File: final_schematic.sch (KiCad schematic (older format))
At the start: 59 parts, among them J1 USB_B_Micro, J2 Conn_Coaxial, J3 Conn_01x04_Male, U1 BQ27441-G1, U2 BQ24075, U3 MTK3339, U4 XC6220B331MR, U5 XC6220B331MR, U6 STM32L476VGTx, U7 RFM95W-868S2, U8 UG-2856KLBAG01_4WSPI, U9 BNO055, X1 SMA_EDGE_UFL

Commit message: made original draft look neater. Now I need to actually do work
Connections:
- wire segments 242 -> 240
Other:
- moved on the sheet: 1.13kOhm1, 1.18kOhm1, 1.5kOhm1, 1.5kOhm2, 4.7uF1, 4.7uF2, 46.4kOhm1, BT1, C1, C10, C11, C12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

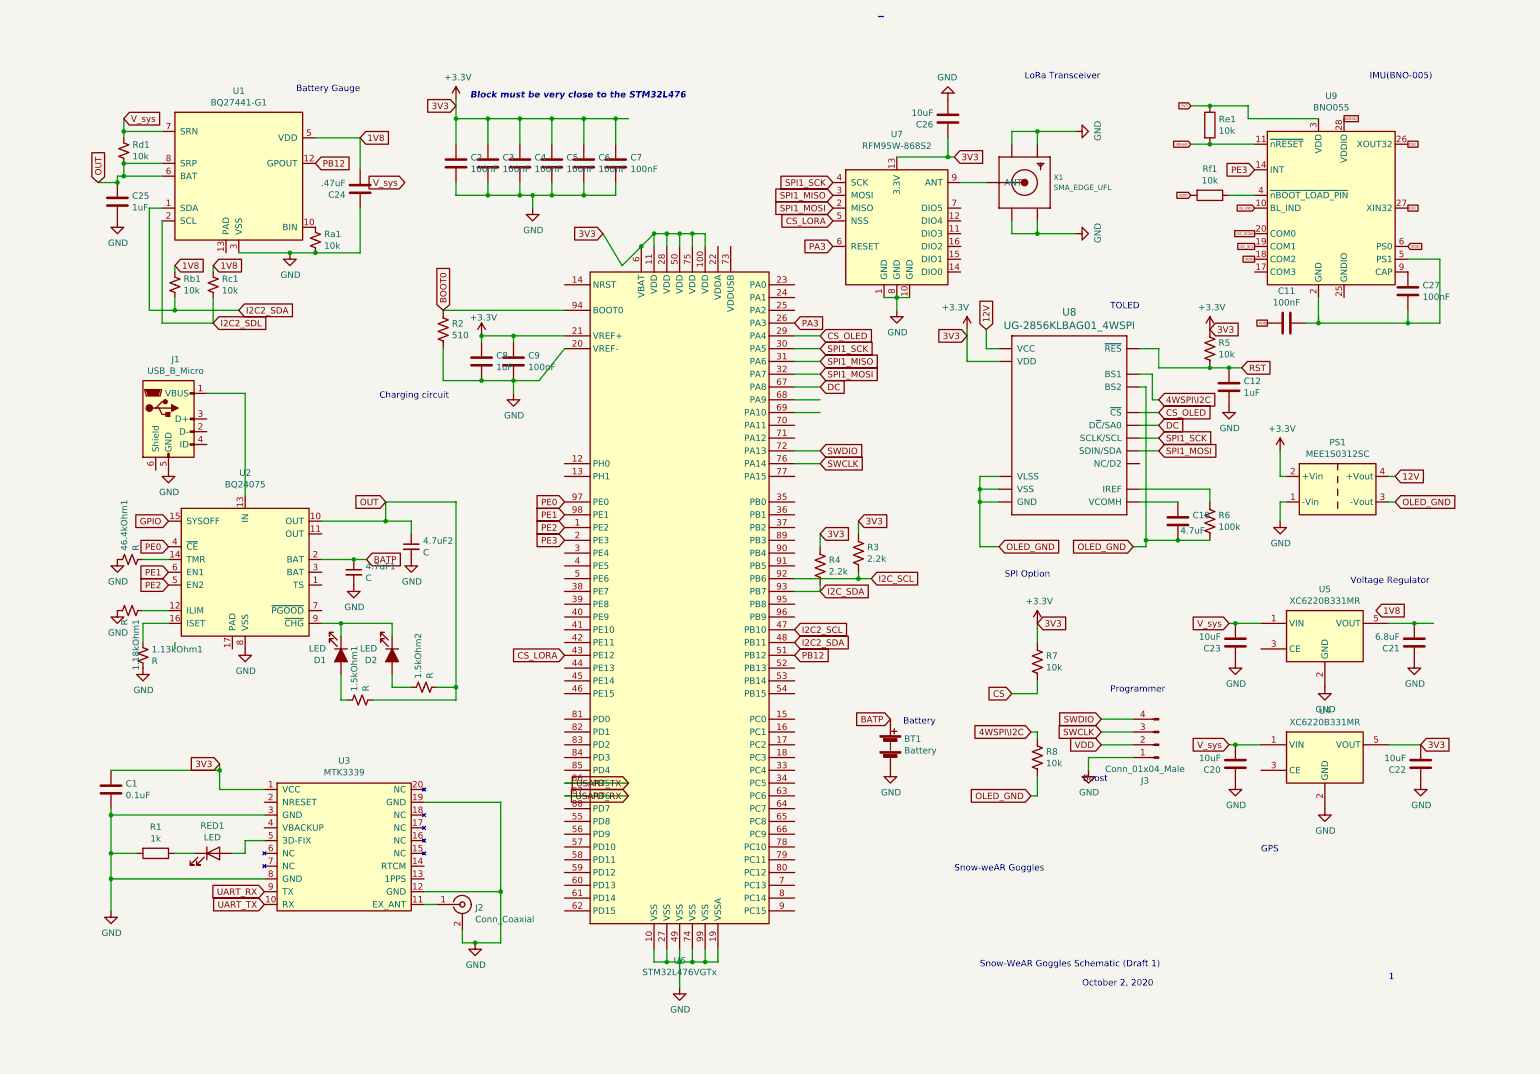
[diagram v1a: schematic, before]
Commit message: Added connectors for battery babysitter and jtag debugger
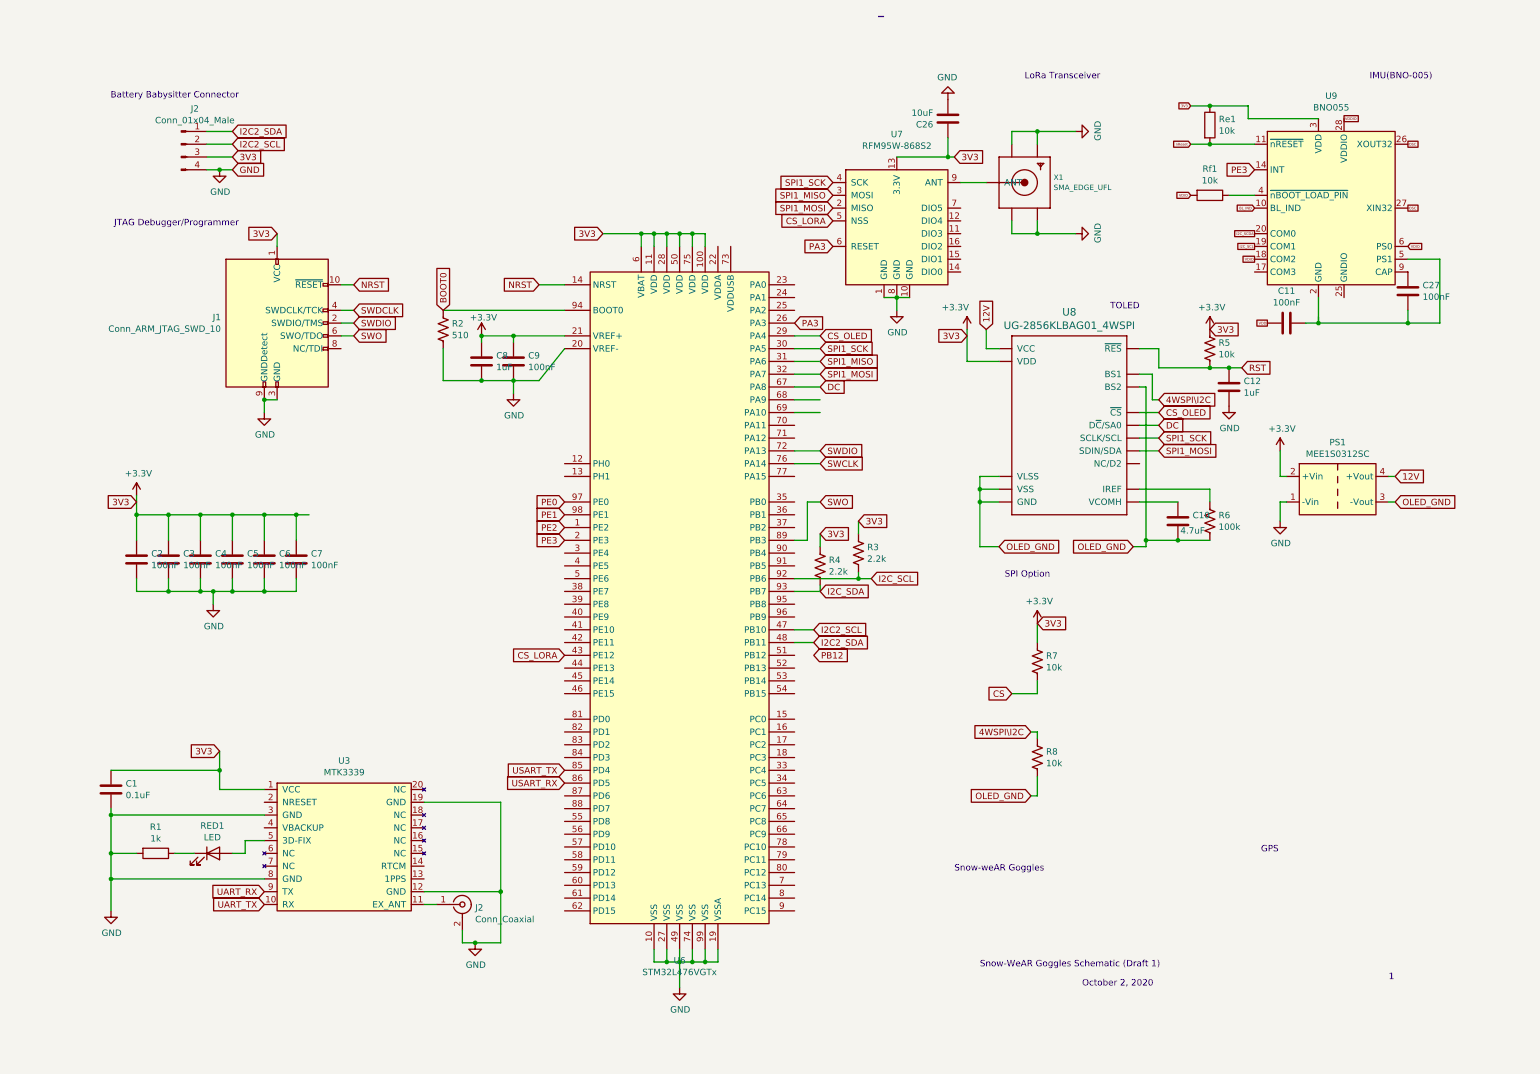
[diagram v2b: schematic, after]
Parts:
- removed 1.13kOhm1, 1.18kOhm1, 1.5kOhm1, 1.5kOhm2, 46.4kOhm1: R, symbol Device:R_Small_US
- removed 4.7uF1, 4.7uF2: C, symbol Device:C_Small
- removed BT1: Battery, symbol Device:Battery
- removed C20, C22, C23: 10uF, symbol Device:C
- removed C21: 6.8uF, symbol Device:C
- removed C24: .47uF, symbol Device:C
- removed C25: 1uF, symbol Device:C
- removed D1, D2: LED, symbol Device:LED_ALT
- removed J1: USB_B_Micro, symbol Connector:USB_B_Micro
- removed J3: Conn_01x04_Male, symbol Connector:Conn_01x04_Male
- removed Ra1, Rb1, Rc1, Rd1: 10k, symbol Device:R_Small_US
- removed U1: BQ27441-G1, Package_SON:Texas_S-PDSO-N12, symbol final_schematic-rescue:BQ27441-G1-Battery_Management_custom
- removed U2: BQ24075, symbol Battery_Management:BQ24075
- removed U4, U5: XC6220B331MR, Package_TO_SOT_SMD:SOT-23-5, symbol final_schematic-rescue:XC6220B331MR-regulator_linear_xc
- added J1: Conn_ARM_JTAG_SWD_10, Connector_PinHeader_1.27mm:PinHeader_2x05_P1.27mm_Vertical_SMD, symbol Connector:Conn_ARM_JTAG_SWD_10
- added J2: Conn_01x04_Male, symbol Connector:Conn_01x04_Male
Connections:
- net labels added: NRST, SWDCLK, SWO
- net labels removed: 1V8, BATP, GPIO, I2C2_SDL, OUT, V_sys
- wire segments 240 -> 193
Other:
- note added: "Battery Babysitter Connector"
- note added: "JTAG Debugger/Programmer"
- note removed: "Battery"
- note removed: "Battery Gauge\n"
- note removed: "Block must be very close to the STM32L476"
- note removed: "Boost"
- note removed: "Charging circuit"
- note removed: "Programmer"
- note removed: "Voltage Regulator\n"
- moved on the sheet: C2, C3, C4, C5, C6, C7

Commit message: added buttons, switch, and 2 leds. Do not have led specs so still need resistor values
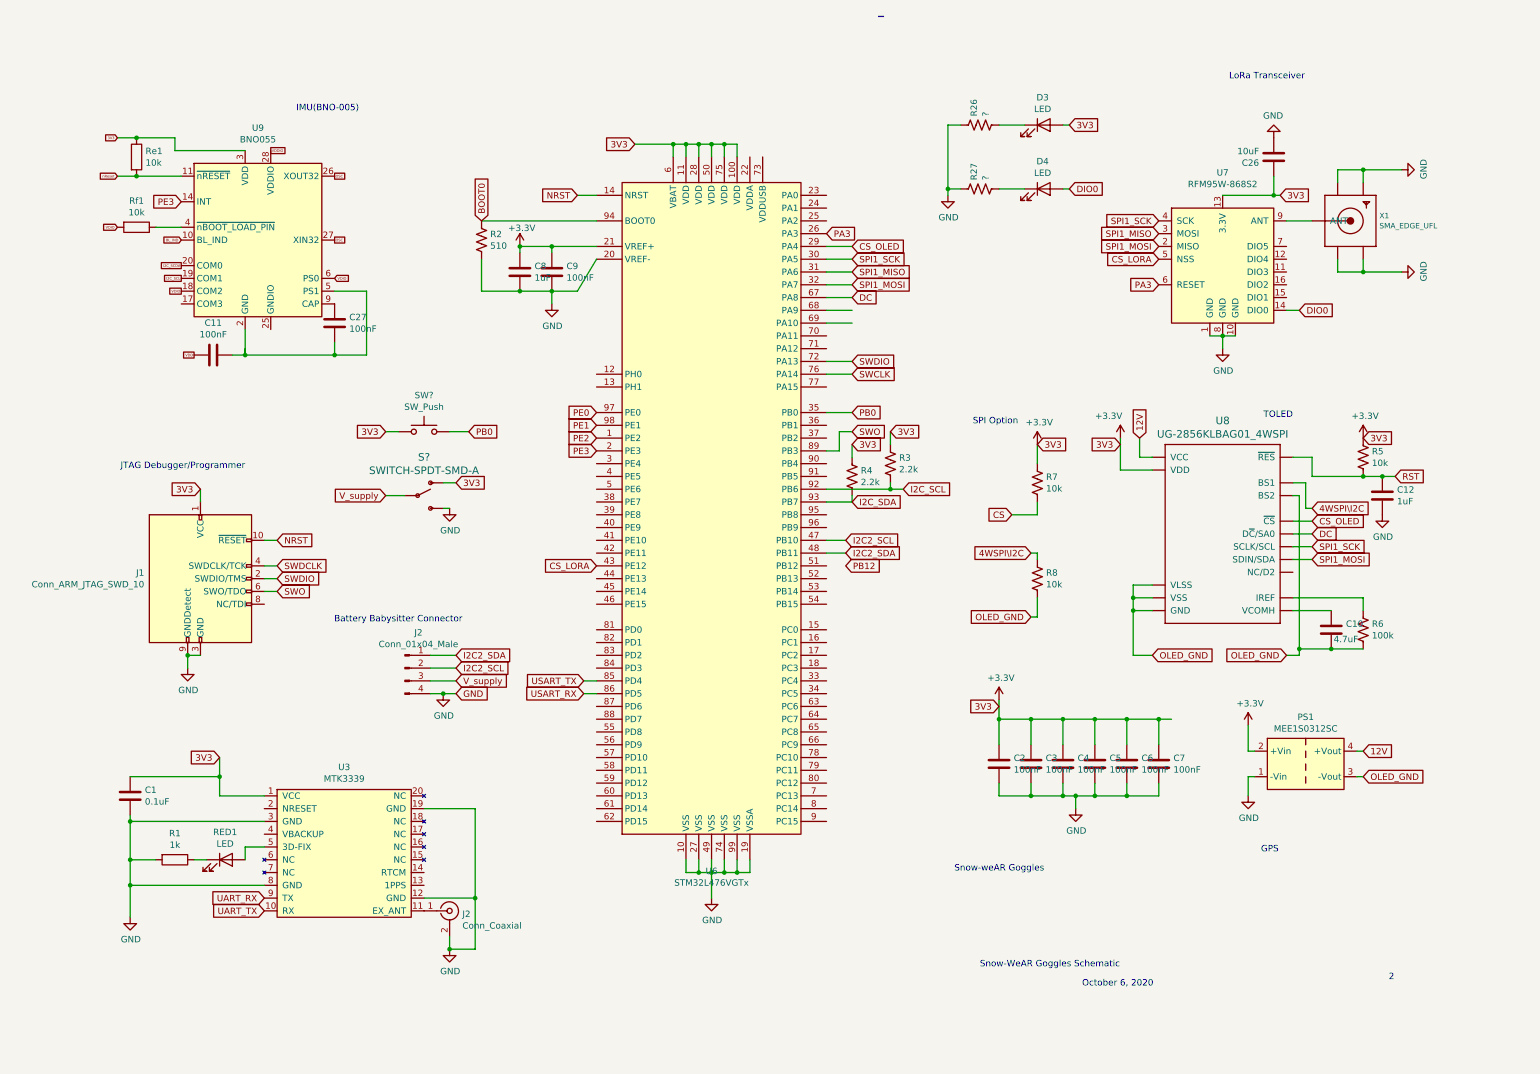
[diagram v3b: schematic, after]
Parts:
- added D3, D4: LED, symbol Device:LED
- added R26, R27: ?, symbol Device:R_US
- added S?: SWITCH-SPDT-SMD-A, symbol schematic-eagle-import:SWITCH-SPDT-SMD-A
- added SW?: SW_Push, symbol Switch:SW_Push
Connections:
- net +3V3: now also D3.2 (A), S?.1 (O), SW?.1; no longer J2.3 (Pin_3)
- net GND: now also R26.1, R27.1, S?.3 (S)
- net DIO0: now reaches U7.14 (DIO0)
- net DIO0: now also D4.2 (A)
- net PB0: now reaches U6.35 (PB0)
- net PB0: now also SW?.2
- new net: D3.1 (K), R26.2
- new net: D4.1 (K), R27.2
- new net V_supply: J2.3 (Pin_3), S?.2 (P)
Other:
- note added: "2"
- note added: "October 6, 2020"
- note added: "Snow-WeAR Goggles Schematic"
- note removed: "1"
- note removed: "October 2, 2020\n"
- note removed: "Snow-WeAR Goggles Schematic (Draft 1)\n"
- moved on the sheet: C1, C10, C11, C12, C2, C26, C27, C3, C4, C5, C6, C7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

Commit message: included session push this time. Still ugly
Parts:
- added SW2: SW_Push, symbol Switch:SW_Push
- gave numbers to parts that had none: 1
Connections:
- net +3V3: now also SW2.1
- net PB1: now reaches U6.36 (PB1)
- net PB1: now also SW2.2
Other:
- moved on the sheet: S?, SW1
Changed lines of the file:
@@
 	6750 3300 6750 3400
 Wire Wire Line
-	6450 3400 6450 3500
+	6450 3450 6450 3500
 Wire Wire Line
 	6750 3700 6750 3750
@@
 Text GLabel 6750 3300 2    50   Input ~ 0
 3V3
-Text GLabel 6450 3400 2    50   Input ~ 0
+Text GLabel 6450 3450 2    50   Input ~ 0
 3V3
 Text Notes 7450 7500 0    50   ~ 0
@@
 Text GLabel 1950 4550 2    50   Input ~ 0
 SWO
-Text GLabel 6450 3300 2    50   Input ~ 0
+Text GLabel 6450 3350 2    50   Input ~ 0
 SWO
 Wire Wire Line
@@
 	9950 2350 9850 2350
 $Comp
-L Switch:SW_Push SW?
+L Switch:SW_Push SW1
 U 1 1 60374032
-P 3100 3300
-F 0 "SW?" H 3100 3585 50  0000 C CNN
-F 1 "SW_Push" H 3100 3494 50  0000 C CNN
-F 2 "" H 3100 3500 50  0001 C CNN
-F 3 "" H 3100 3500 50  0001 C CNN
-	1    3100 3300
+P 3250 3450
+F 0 "SW1" H 3250 3735 50  0000 C CNN
+F 1 "SW_Push" H 3250 3644 50  0000 C CNN
+F 2 "" H 3250 3650 50  0001 C CNN
+F 3 "" H 3250 3650 50  0001 C CNN
+	1    3250 3450
 	1    0    0    -1
 $EndComp
@@
 L schematic-eagle-import:SWITCH-SPDT-SMD-A S?
 U 1 1 60374331
-P 3050 3800
-F 0 "S?" H 3100 4101 59  0000 C CNN
-F 1 "SWITCH-SPDT-SMD-A" H 3100 3996 59  0000 C CNN
-F 2 "" H 3050 3800 50  0001 C CNN
-F 3 "" H 3050 3800 50  0001 C CNN
-	1    3050 3800
+P 3200 3950
+F 0 "S?" H 3250 4251 59  0000 C CNN
+F 1 "SWITCH-SPDT-SMD-A" H 3250 4146 59  0000 C CNN
+F 2 "" H 3200 3950 50  0001 C CNN
+F 3 "" H 3200 3950 50  0001 C CNN
+	1    3200 3950
 	1    0    0    -1
 $EndComp
@@
 L power:GND #PWR?
 U 1 1 6038CE54
-P 3300 3900
-F 0 "#PWR?" H 3300 3650 50  0001 C CNN
-F 1 "GND" H 3305 3727 50  0000 C CNN
-F 2 "" H 3300 3900 50  0001 C CNN
-F 3 "" H 3300 3900 50  0001 C CNN
-	1    3300 3900
-	1    0    0    -1
-$EndComp
-Text GLabel 2800 3800 0    50   Input ~ 0
+P 3450 4050
+F 0 "#PWR?" H 3450 3800 50  0001 C CNN
+F 1 "GND" H 3455 3877 50  0000 C CNN
+F 2 "" H 3450 4050 50  0001 C CNN
+F 3 "" H 3450 4050 50  0001 C CNN
+	1    3450 4050
+	1    0    0    -1
+$EndComp
+Text GLabel 2950 3950 0    50   Input ~ 0
 V_supply
-Text GLabel 3350 3700 2    50   Input ~ 0
-3V3
-Wire Wire Line
-	2800 3800 2950 3800
-Wire Wire Line
-	3250 3700 3350 3700
-Wire Wire Line
-	3300 3900 3250 3900
-Wire Wire Line
-	6450 3300 6350 3300
-Wire Wire Line
-	6350 3300 6350 3450
+Text GLabel 3500 3850 2    50   Input ~ 0
+3V3
+Wire Wire Line
+	2950 3950 3100 3950
+Wire Wire Line
+	3400 3850 3500 3850
+Wire Wire Line
+	3450 4050 3400 4050
 Text GLabel 6450 3150 2    50   Input ~ 0
 PB0
 Wire Wire Line
 	6450 3150 6250 3150
-Text GLabel 2800 3300 0    50   Input ~ 0
-3V3
-Text GLabel 3450 3300 2    50   Input ~ 0
+Text GLabel 2950 3450 0    50   Input ~ 0
+3V3
+Text GLabel 3600 3450 2    50   Input ~ 0
 PB0
 Wire Wire Line
-	2800 3300 2900 3300
-Wire Wire Line
-	3300 3300 3450 3300
+	2950 3450 3050 3450
+Wire Wire Line
+	3450 3450 3600 3450
+Text GLabel 6450 3250 2    50   Input ~ 0
+PB1
+Wire Wire Line
+	6350 3450 6350 3350
+Wire Wire Line
+	6350 3350 6450 3350
+Wire Wire Line
+	6450 3250 6250 3250
+$Comp
+L Switch:SW_Push SW2
+U 1 1 6050A466
+P 3250 3050
+F 0 "SW2" H 3250 3335 50  0000 C CNN
+F 1 "SW_Push" H 3250 3244 50  0000 C CNN
+F 2 "" H 3250 3250 50  0001 C CNN
+F 3 "" H 3250 3250 50  0001 C CNN
+	1    3250 3050
+	1    0    0    -1
+$EndComp
+Wire Wire Line
+	2950 3050 3050 3050
+Wire Wire Line
+	3450 3050 3600 3050
+Text GLabel 2950 3050 0    50   Input ~ 0
+3V3
+Text GLabel 3600 3050 2    50   Input ~ 0
+PB1
 $EndSCHEMATC

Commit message: hi Kennedy
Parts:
- added C3, C5, C6: 1uF, symbol Device:C
- added R2, R3, R5: 10k, symbol Device:R_US
- added SW3: SW_Push, symbol Switch:SW_Push
- gave numbers to parts that had none: 1
- renumbered C3 to C10, C4 to C11, C5 to C12, C6 to C13, C7 to C14, C26 to C15, C10 to C16, C12 to C17, C11 to C2, C27 to C4, C8 to C7, C9 to C8, C2 to C9, D3 to D1, D4 to D2, J2 to J3, R7 to R10, R8 to R11, R5 to R12, R6 to R13, R2 to R4, R4 to R6, R3 to R7, R26 to R8, R27 to R9, U9 to U1, U3 to U2, U6 to U3, U7 to U4, U8 to U5
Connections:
- net I2C_SCDA is gone; now on net I2C_SDA: U1.20 (COM0)
- net SWDCLK is gone; now on net SWCLK: J1.4 (SWDCLK/TCK)
- net UART_RX is gone; now on net USART_RX: U2.9 (TX)
- net UART_TX is gone; now on net USART_TX: U2.10 (RX)
- net +3V3: now also R2.1, R3.1, R5.1; no longer SW1.1, SW2.1
- net GND: now also SW1.2, SW2.2, C3.1, C5.1, C6.1, SW3.2
- net NRST: now also C6.2, R5.2, SW3.1
- net PB0: now also SW1.1, C3.2, R2.2; no longer SW1.2
- net PB1: now also SW2.1, C5.2, R3.2; no longer SW2.2
- net PB12: now also U3.51 (PB12)
- net PE0: no longer names the net of U3.97 (PE0)
- net PE1: no longer names the net of U3.98 (PE1)
- net PE2: no longer names the net of U3.1 (PE2)
- no-connect marks 0 -> 73
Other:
- moved on the sheet: C2, C4, Re1, Rf1, S1, U1

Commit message: last minute backup before adding oled headers
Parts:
- added C? (x2): 120nF, symbol Device:C
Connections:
- net CS is gone; now on net CS_OLED: R10.2
- net VDD is gone; now on net +3V3: C2.1
- net VDDIO is gone; now on net +3V3: U1.28 (VDDIO)
- net nReset is gone; now on net PE0: Re1.2, U1.11 (~nRESET)
- net +3V3: now also Rf1.2, C?.1, C?.1
- net GND: now also C2.2, C4.2, U1.15 (GNDIO), U1.16 (GNDIO), U1.18 (COM2), U1.2 (GND), U1.25 (GNDIO), U1.5 (PS1), U1.6 (PS0), C?.2, C?.2
- net PE0: now reaches U3.97 (PE0)
- net BL_IND: no longer names the net of U1.10 (BL_IND)
- net OSC: no longer names the net of U1.26 (XOUT32)
- net OSC: no longer U1.27 (XIN32)
- removed net VDIO: Rf1.2, U1.18 (COM2), U1.6 (PS0)
- no-connect marks 73 -> 71
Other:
- moved on the sheet: C6, J2, R5, S1, SW3

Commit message: schematic finalized
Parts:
- removed C16: 4.7uF, symbol Device:C
- removed C17: 1uF, symbol Device:C
- removed PS1: MEE1S0312SC, Converter_DCDC:Converter_DCDC_Murata_MEE1SxxxxSC_THT, symbol Converter_DCDC1:MEE1S0312SC
- removed R10, R11, R12: 10k, symbol Device:R_US
- removed R13: 100k, symbol Device:R_US
- removed U5: UG-2856KLBAG01_4WSPI, symbol schematic_kennedyUpdate-cache:schematic_kennedyUpdate-rescue_UG-2856KLBAG01_4WS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
- added C8: 1uF, symbol Device:C
- added J1: Conn_Male, symbol Connector:Conn_01x06_Male
- added J2, J5, J8: Conn_Male, symbol Connector:Conn_01x01_Male
- added J4: Conn_01x02_Male, symbol Connector:Conn_01x02_Male
- added R5: 10k, symbol Device:R_US
- gave numbers to parts that had none: 2
- renumbered C7 to C10, C8 to C11, C9 to C12, C10 to C13, C11 to C14, C12 to C15, C13 to C16, C14 to C17, C15 to C18, C6 to C2, C5 to C4, C2 to C5, C4 to C6, J2 to J3, J3 to J6, J1 to J7, R9 to R10, R5 to R2, R2 to R3, R3 to R4, R4 to R6, R6 to R7, R7 to R8, R8 to R9, SW3 to SW1, SW1 to SW2, SW2 to SW3
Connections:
- net BOOT0: now also J8.1 (Pin_1)
- net CS_OLED: now also J1.6 (Pin_6)
- net GND: now also C8.2, J1.1 (Pin_1); no longer X1.GND@3 (GND3), X1.GND@4 (GND4)
- net PB12: now also J4.1 (Pin_1)
- net SPI1_MOSI: now also J1.3 (Pin_3)
- net SPI1_SCK: now also J1.4 (Pin_4)
- net PH1: now reaches U1.10 (BL_IND)
- net PH1: now also U3.13 (PH1)
- net PH0: now reaches U1.17 (COM3)
- net PH0: now also U3.12 (PH0)
- net PB13: now reaches U3.52 (PB13)
- net PB13: now also J4.2 (Pin_2)
- net PB14: now reaches U3.53 (PB14)
- net PB14: now also J5.1 (Pin_1)
- net +3V3 renamed 3V3
- net 3V3: now also J1.2 (Pin_2), R5.1
- net DC renamed DC_OLED
- net DC_OLED: now also J1.5 (Pin_5)
- new net: X1.GND@3 (GND3), X1.GND@4 (GND4)
- new net: C8.1, J2.1 (Pin_1), R5.2
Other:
- note added: "Radio pushbutton"
- note added: "Reset pushbutton"
- note added: "Session pushbutton"
- note removed: "SPI Option"
- note removed: "TOLED"
- moved on the sheet: C1, C12, C13, C14, C15, C16, C17, C18, C2, C3, C4, D1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
